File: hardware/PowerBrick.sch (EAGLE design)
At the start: 13 parts, among them Q1 SI2308BDS-T1-GE3, U1 MC1525TT, U2 PIC12F675SN, U3 BD6221

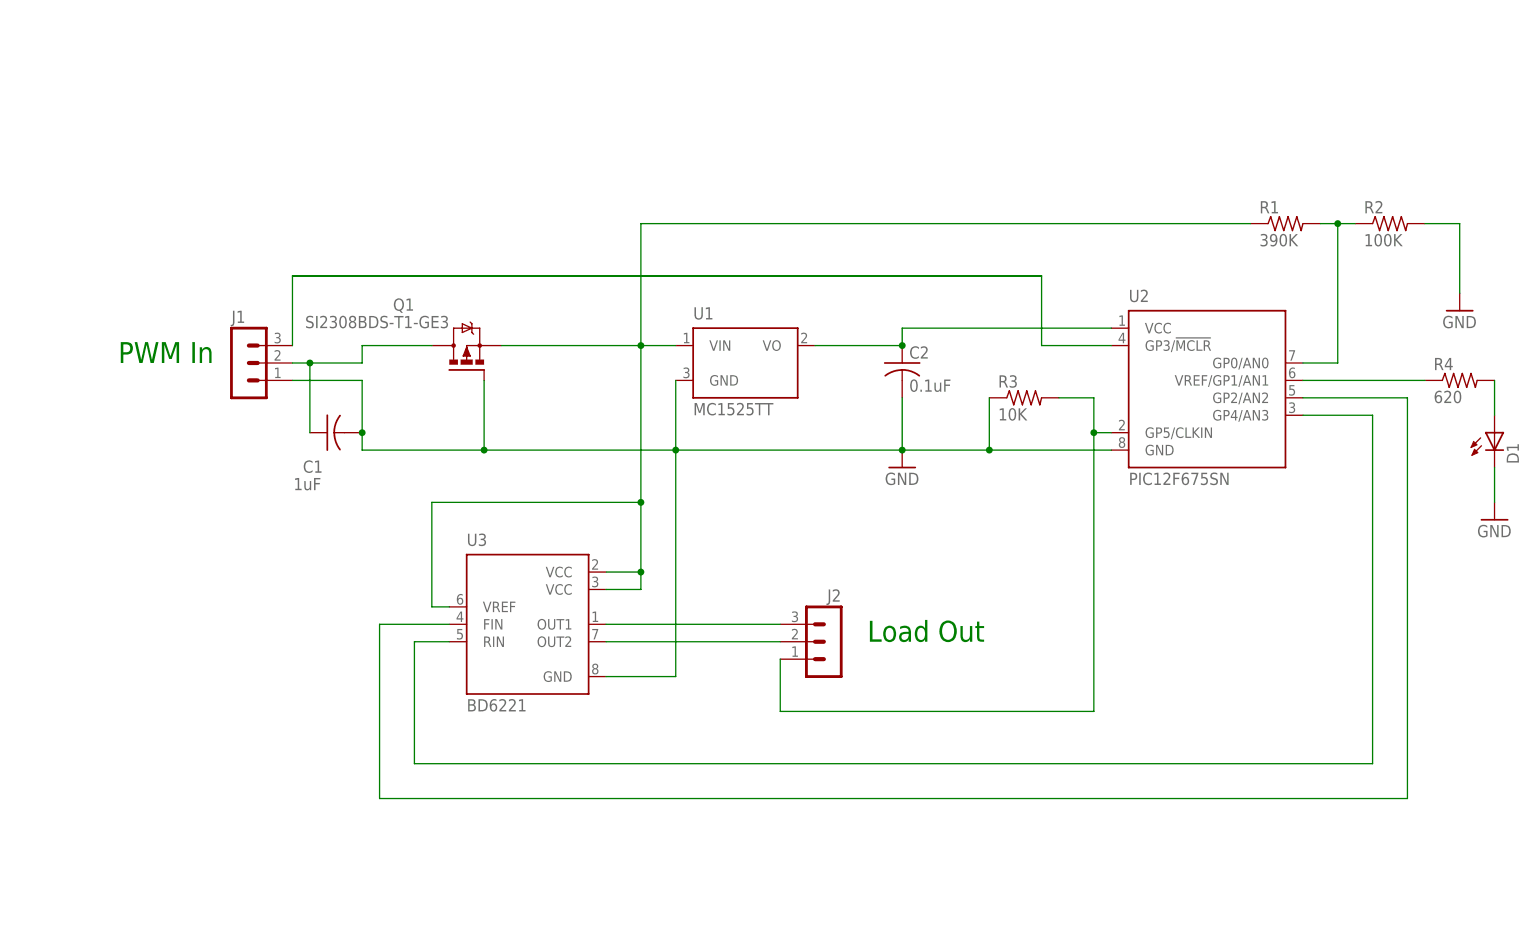
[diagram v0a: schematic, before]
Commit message: Added optional level shift transistor on the receiver PWM input
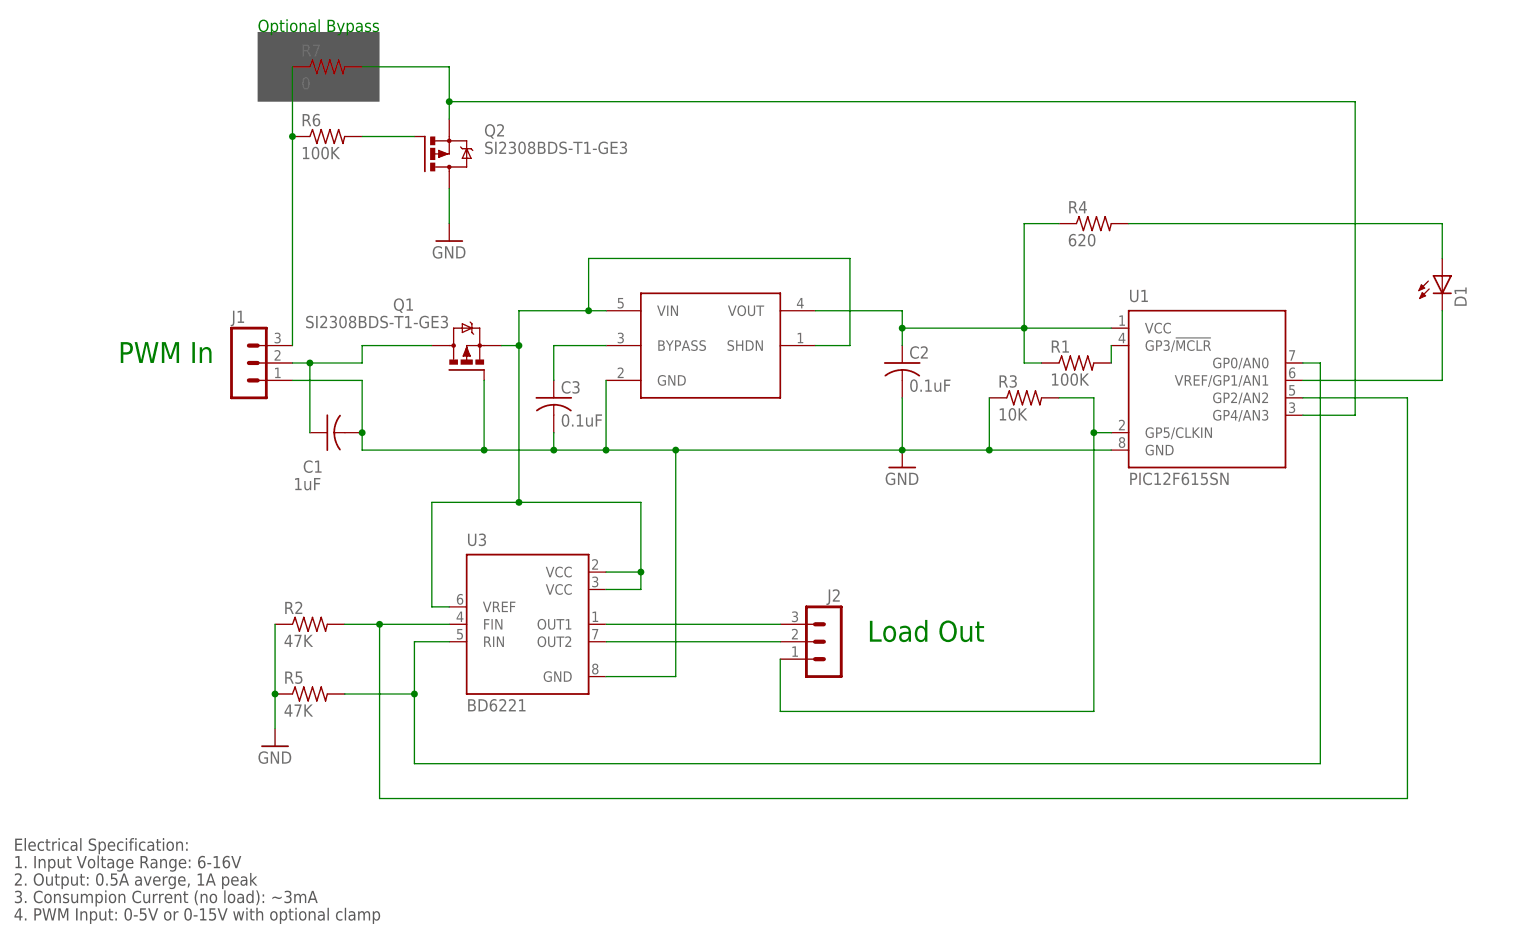
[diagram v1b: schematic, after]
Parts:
- added C3: 0.1uF, rcl:C-USC0805
- added Q2: SI2308BDS-T1-GE3, transistor-power:IRLML5203
- added R5: 47K, resistor:R-US_R0603
- added R6: 100K, resistor:R-US_R0603
- added R7: 0, resistor:R-US_R0603
- R1: value 390K -> 100K
- R2: value 100K -> 47K
- U1: value MC1525TT -> PIC12F615SN; device microchip:MC1525TT -> personal:PIC12H615SN
- U2: value PIC12F675SN -> LK112M50TR; device microchip:PIC12F675SN -> personal:LK112M50TR
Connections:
- removed net N$8 (its old number): R4.1, U2.VREF/GP1/AN1
- new net N$11: R1.2, U1.GP3/!MCLR
- new net N$12: Q2.G, R6.2
- new net N$13: J1.3, R6.1, R7.1
- new net N$15: C3.1, U2.BYPASS
- net GND: now also C3.2, Q2.D, R2.1, R5.1; no longer D1.C, R2.2
- net J1: now also Q2.S, R7.2, U1.GP4/AN3; no longer J1.3, U2.GP3/!MCLR
- net N$1: now also U1.GP5/CLKIN; no longer U2.GP5/CLKIN
- net N$2: now also U2.SHDN, U2.VIN; no longer R1.1, U1.VIN
- net N$3: now also R1.1, R4.1, U1.VCC, U2.VOUT; no longer U1.VO, U2.VCC
- net N$6: now also R2.2, U1.GP2/AN2; no longer U2.GP2/AN2
- net N$7: now also R5.2, U1.GP0/AN0; no longer U2.GP4/AN3
- net N$9: now also D1.C, U1.VREF/GP1/AN1; no longer R1.2, R2.1, U2.GP0/AN0
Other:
- note added: "1. Input Voltage Range: 6-16V"
- note added: "2. Output: 0.5A averge, 1A peak"
- note added: "3. Consumpion Current (no load): ~3mA"
- note added: "4. PWM Input: 0-5V or 0-15V with optional clamp"
- note added: "Electrical Specification:"
- note added: "Optional Bypass"
- moved on the sheet: D1, R1, R2, R4
